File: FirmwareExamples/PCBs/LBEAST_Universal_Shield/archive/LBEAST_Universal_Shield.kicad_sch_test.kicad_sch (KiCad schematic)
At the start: 53 parts, among them J1 MTJ-883X1, J10 CAN BUS, J11 JST-XH 2-Pin Fan, J2 MTJ-883X1, J3 MTJ-883X1, J4 MTJ-883X1, J5 MTJ-883X1, J6 MTJ-883X1, J7 MTJ-883X1, J8 MTJ-883X1, J9 Barrel_Jack_Switch, Q1 IRF9540N, Q2 IRLZ44N, SW1 SW_DIP_x01, U2 LM2576HVS-5-LBEAST, U5 LAN8720A, U8 ADM3057ExRW, Y1 25MHz

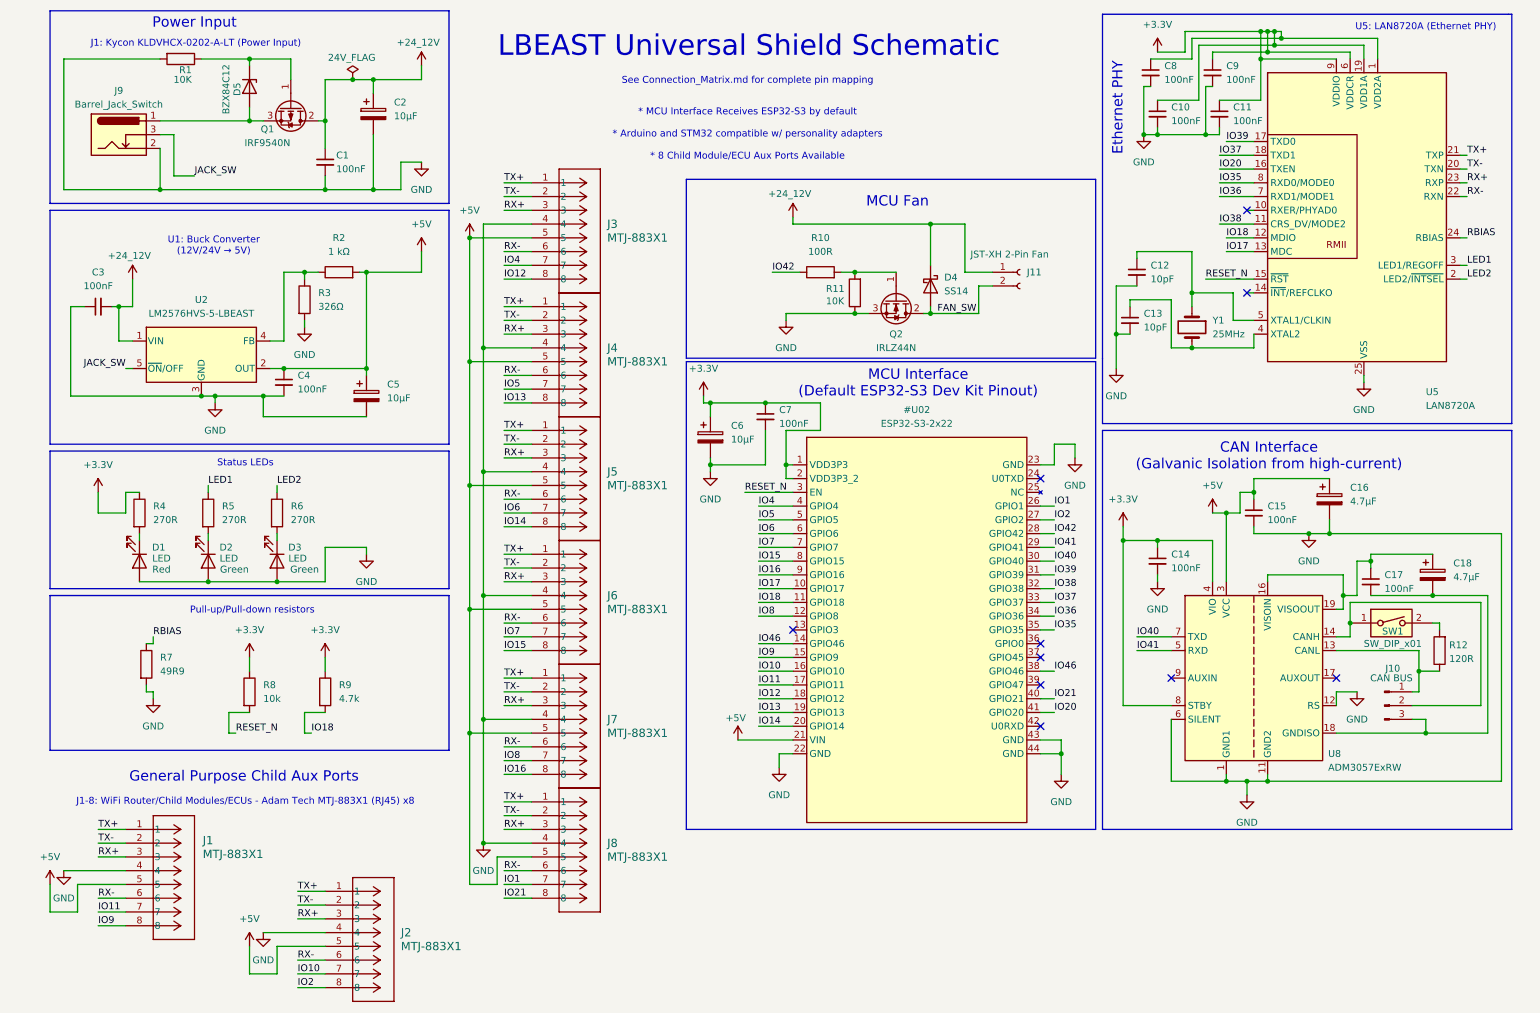
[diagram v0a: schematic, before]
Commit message: add alpha universal shield schematic
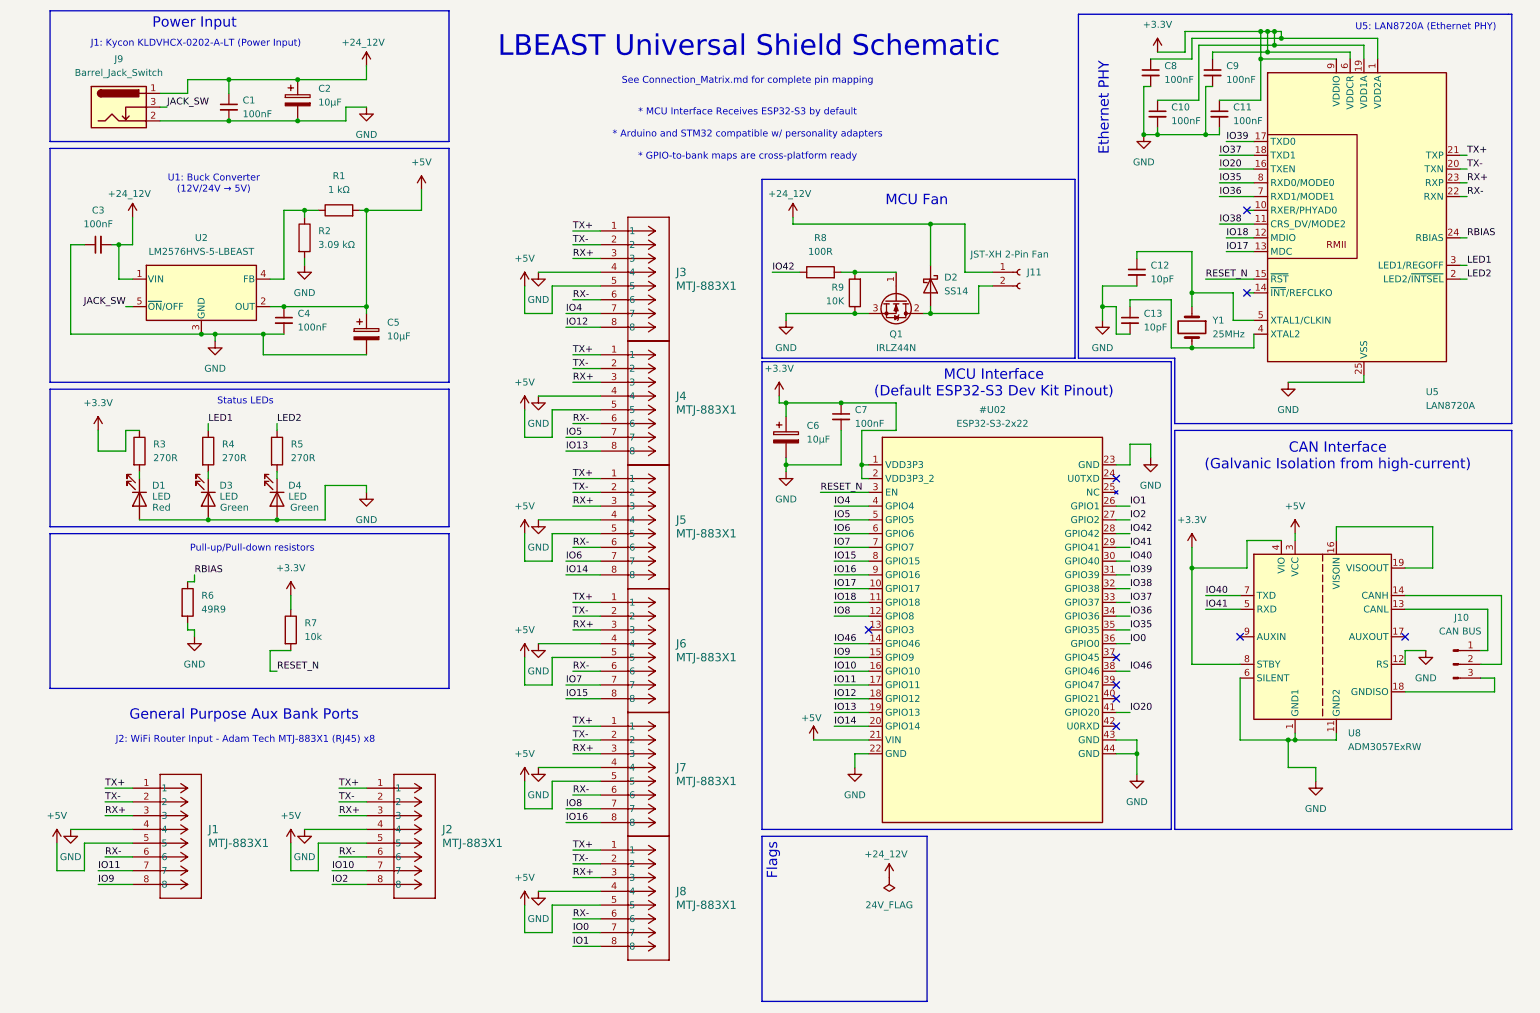
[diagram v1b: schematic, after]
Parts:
- removed C14, C15, C17: 100nF, Capacitor_SMD:C_0805_2012Metric, symbol Device:C_Small
- removed C16, C18: 4.7µF, Capacitor_Tantalum_SMD:CP_EIA-3216-18_Kemet-A, symbol Device:C_Polarized
- removed D5: BZX84C12, Package_TO_SOT_SMD:SOT-23, symbol Diode:BZX84Cxx
- removed Q1: IRF9540N, Package_TO_SOT_THT:TO-220-3_Vertical, symbol Transistor_FET:IRF9540N
- removed R1: 10K, Resistor_SMD:R_0805_2012Metric, symbol Device:R
- removed R12: 120R, Resistor_SMD:R_0805_2012Metric, symbol Device:R
- removed R9: 4.7k, Resistor_SMD:R_0805_2012Metric, symbol Device:R
- removed SW1: SW_DIP_x01, symbol Switch:SW_DIP_x01
- J10: footprint LBEASTLibrary:JST_XH_B3B-XH-A_1x03_P2.50mm_Vertical -> (none)
- R2: renamed from R3; value 326Ω -> 3.09 kΩ
- renumbered D4 to D2, D2 to D3, D3 to D4, Q2 to Q1, R2 to R1, R4 to R3, R5 to R4, R6 to R5, R7 to R6, R8 to R7, R10 to R8, R11 to R9
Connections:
- net IO21 is gone; now on net IO1: J8.8
- net +24_12V: now also J9.1
- net IO1: no longer J8.7
- net FAN_SW: no longer names the net of D2.2 (A), J11.2 (Pin_2), Q1.2 (D)
- new net IO0: J8.7
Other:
- note added: "* MCU Interface Receives ESP32-S3 by default * Arduino and STM32 compatible w/ personality adapters * GPIO-to-bank maps are cross-platform ready"
- note added: "Flags"
- note added: "General Purpose Aux Bank Ports"
- note added: "J2: WiFi Router Input - Adam Tech MTJ-883X1 (RJ45) x8"
- note removed: "* MCU Interface Receives ESP32-S3 by default * Arduino and STM32 compatible w/ personality adapters * 8 Child Module/ECU Aux Ports Available"
- note removed: "General Purpose Child Aux Ports"
- note removed: "J1-8: WiFi Router/Child Modules/ECUs - Adam Tech MTJ-883X1 (RJ45) x8"
- moved on the sheet: C1, C2, C3, C4, C5, C6, C7, D1, D3, D4, J1, J10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
